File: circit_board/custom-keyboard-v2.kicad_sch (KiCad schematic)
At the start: 1 part

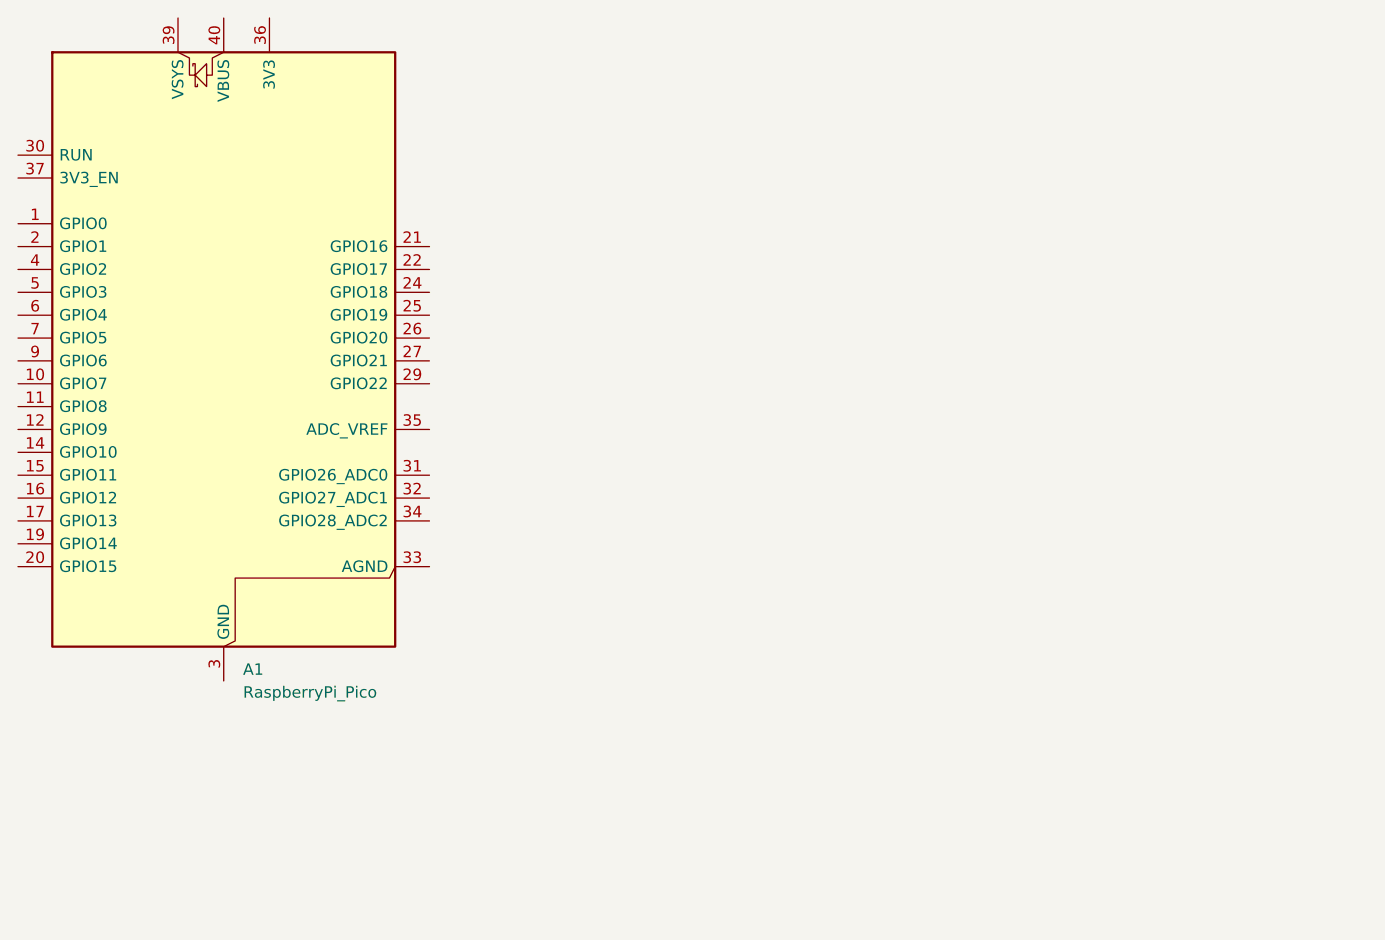
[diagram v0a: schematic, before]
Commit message: Added kicad library for key switches + added a few components into the design
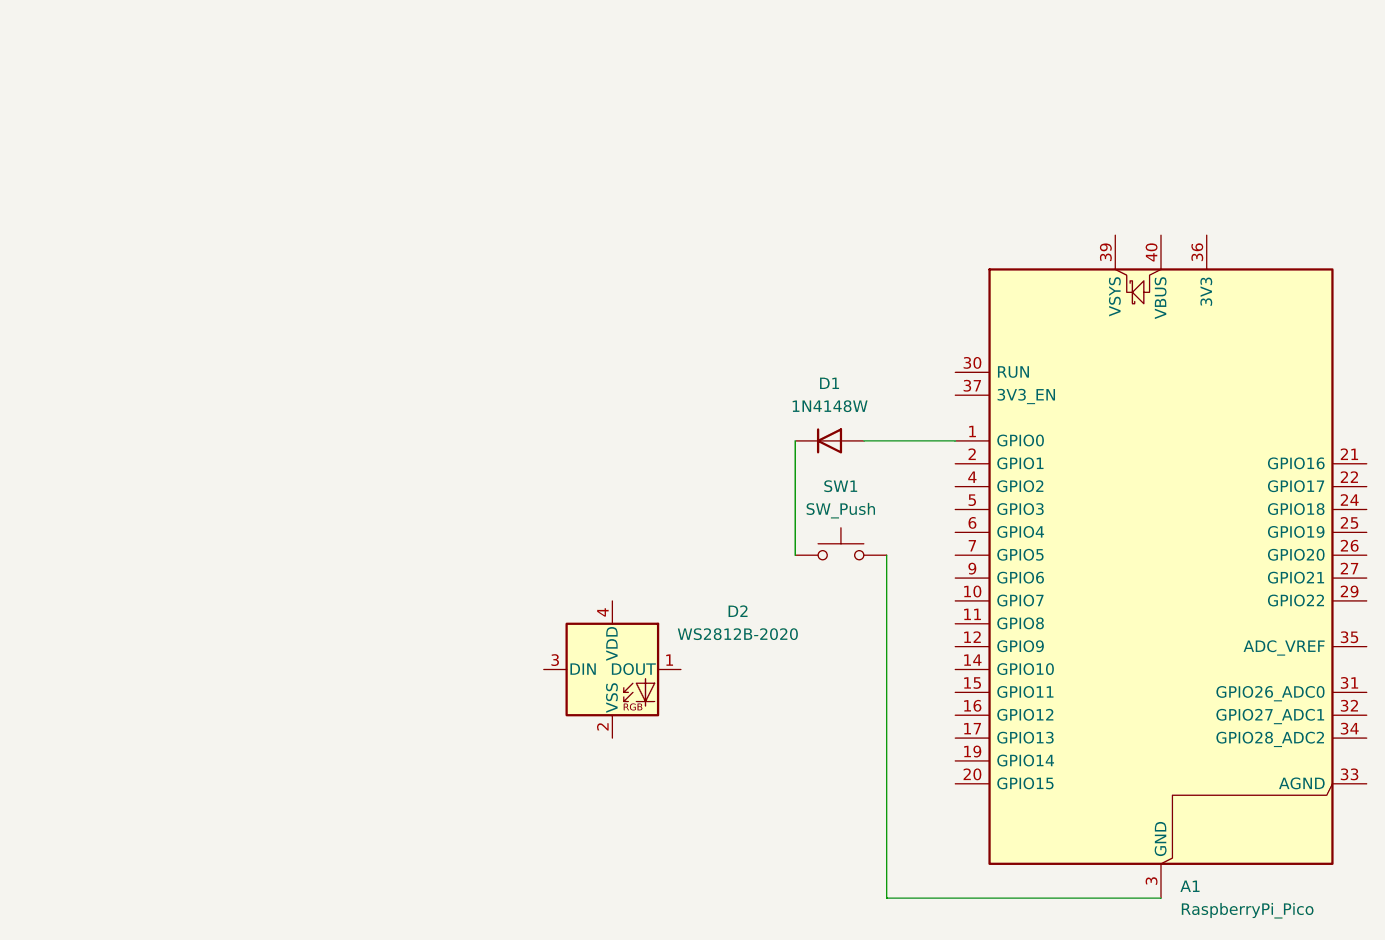
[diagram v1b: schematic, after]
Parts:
- added D1: 1N4148W, Diode_SMD:D_SOD-123, symbol Diode:1N4148W
- added D2: WS2812B-2020, LED_SMD:LED_WS2812B-2020_PLCC4_2.0x2.0mm, symbol LED:WS2812B-2020
- added SW1: SW_Push, MX_V2:Gateron-KS33-Solderable-Template, symbol Switch:SW_Push
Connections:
- net at A1.1 (GPIO0): now also D1.2 (A)
- net at A1.13 (GND), A1.18 (GND), A1.23 (GND)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: now also SW1.2
- new net: D1.1 (K), SW1.1
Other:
- moved on the sheet: A1

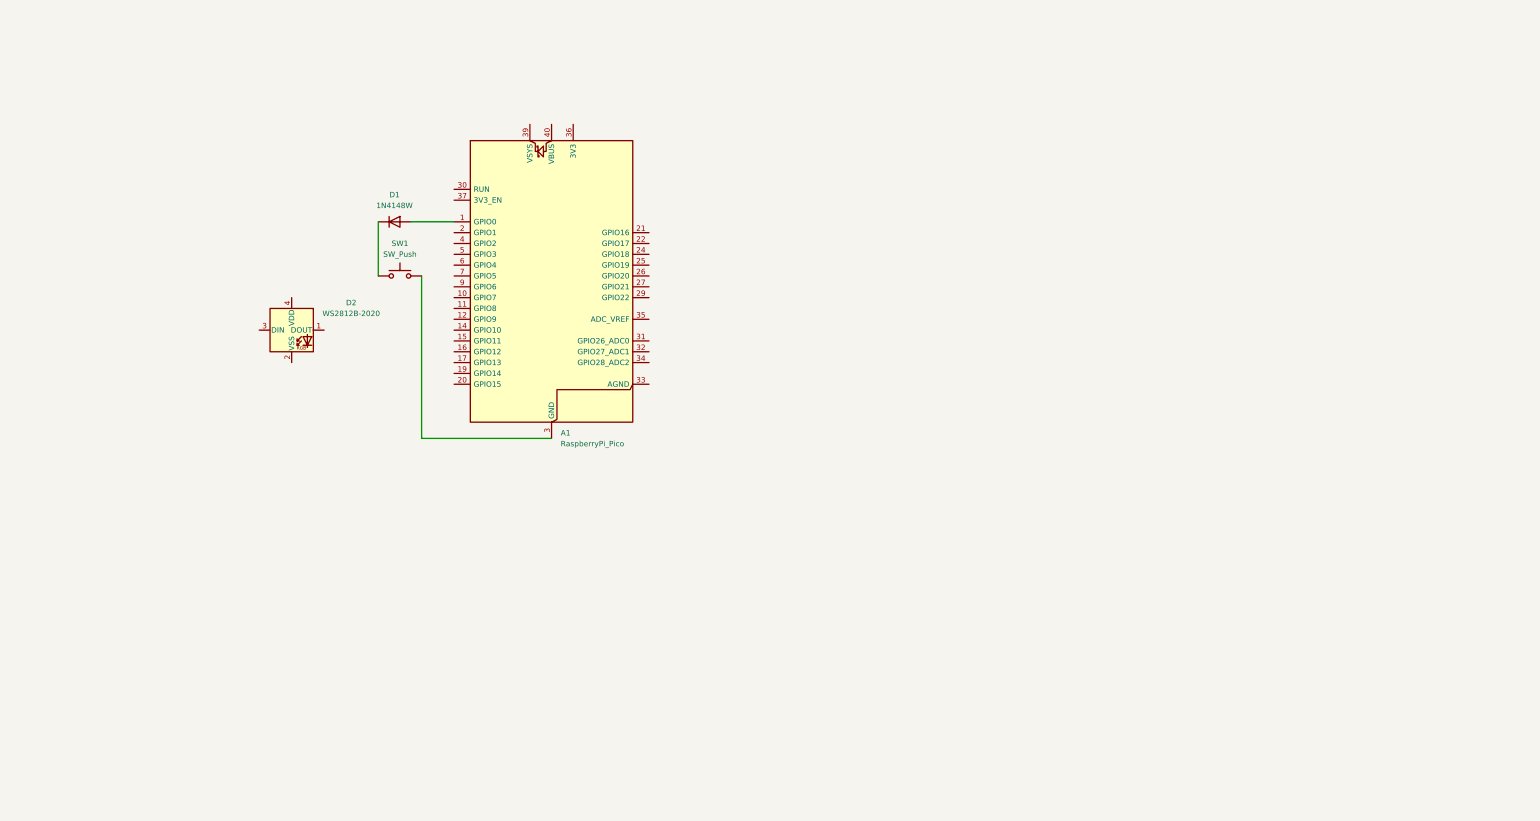
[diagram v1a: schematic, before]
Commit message: Added keyboard matrix to circit schematic
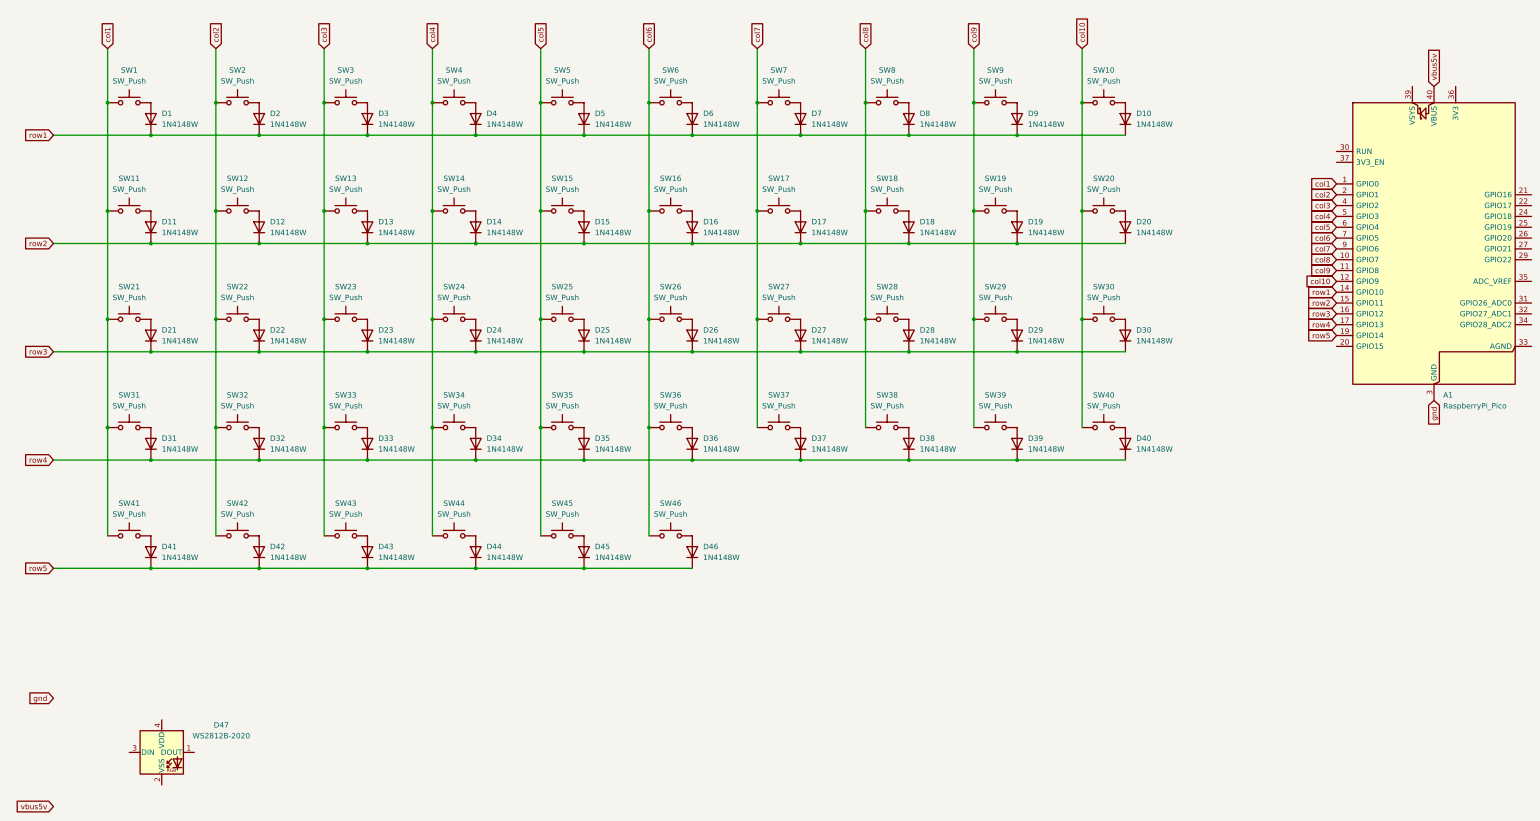
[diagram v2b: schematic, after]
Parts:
- removed D2: WS2812B-2020, LED_SMD:LED_WS2812B-2020_PLCC4_2.0x2.0mm, symbol LED:WS2812B-2020
- added D10, D11, D12, D13, D14, D15, D16, D17, D18, D19, D2, D20, D21, D22, D23, D24, D25, D26, D27, D28, D29, D3, D30, D31, D32, D33, D34, D35, D36, D37, D38, D39, D4, D40, D41, D42, D43, D44, D45, D46, D5, D6, D7, D8, D9: 1N4148W, Diode_SMD:D_SOD-123, symbol Diode:1N4148W
- added D47: WS2812B-2020, LED_SMD:LED_WS2812B-2020_PLCC4_2.0x2.0mm, symbol LED:WS2812B-2020
- added SW10, SW11, SW12, SW13, SW14, SW15, SW16, SW17, SW18, SW19, SW2, SW20, SW21, SW22, SW23, SW24, SW25, SW26, SW27, SW28, SW29, SW3, SW30, SW31, SW32, SW33, SW34, SW35, SW36, SW37, SW38, SW39, SW4, SW40, SW41, SW42, SW43, SW44, SW45, SW46, SW5, SW6, SW7, SW8, SW9: SW_Push, MX_V2:Gateron-KS33-Solderable-Template, symbol Switch:SW_Push
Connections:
- net col1: now reaches SW1.1
- net col1: now also A1.1 (GPIO0), SW11.1, SW21.1, SW31.1, SW41.1; no longer D1.1 (K)
- net at D1.2 (A): now also SW1.2; no longer A1.1 (GPIO0)
- net gnd: now reaches A1.13 (GND), A1.18 (GND), A1.23 (GND), A1.28 (GND), A1.3 (GND), A1.38 (GND), A1.8 (GND)
- net gnd: no longer SW1.2
- net col8: now reaches A1.10 (GPIO7)
- net col8: now also SW18.1, SW28.1, SW38.1, SW8.1
- net col9: now reaches A1.11 (GPIO8)
- net col9: now also SW19.1, SW29.1, SW39.1, SW9.1
- net col10: now reaches A1.12 (GPIO9)
- net col10: now also SW10.1, SW20.1, SW30.1, SW40.1
- net row1: now reaches A1.14 (GPIO10)
- net row1: now also D1.1 (K), D10.1 (K), D2.1 (K), D3.1 (K), D4.1 (K), D5.1 (K), D6.1 (K), D7.1 (K), D8.1 (K), D9.1 (K)
- net row2: now reaches A1.15 (GPIO11)
- net row2: now also D11.1 (K), D12.1 (K), D13.1 (K), D14.1 (K), D15.1 (K), D16.1 (K), D17.1 (K), D18.1 (K), D19.1 (K), D20.1 (K)
- net row3: now reaches A1.16 (GPIO12)
- net row3: now also D21.1 (K), D22.1 (K), D23.1 (K), D24.1 (K), D25.1 (K), D26.1 (K), D27.1 (K), D28.1 (K), D29.1 (K), D30.1 (K)
- net row4: now reaches A1.17 (GPIO13)
- net row4: now also D31.1 (K), D32.1 (K), D33.1 (K), D34.1 (K), D35.1 (K), D36.1 (K), D37.1 (K), D38.1 (K), D39.1 (K), D40.1 (K)
- net row5: now reaches A1.19 (GPIO14)
- net row5: now also D41.1 (K), D42.1 (K), D43.1 (K), D44.1 (K), D45.1 (K), D46.1 (K)
- net col2: now reaches A1.2 (GPIO1)
- net col2: now also SW12.1, SW2.1, SW22.1, SW32.1, SW42.1
- net col3: now reaches A1.4 (GPIO2)
- net col3: now also SW13.1, SW23.1, SW3.1, SW33.1, SW43.1
- net vbus5v: now reaches A1.40 (VBUS)
- net col4: now reaches A1.5 (GPIO3)
- net col4: now also SW14.1, SW24.1, SW34.1, SW4.1, SW44.1
- net col5: now reaches A1.6 (GPIO4)
- net col5: now also SW15.1, SW25.1, SW35.1, SW45.1, SW5.1
- net col6: now reaches A1.7 (GPIO5)
- net col6: now also SW16.1, SW26.1, SW36.1, SW46.1, SW6.1
- net col7: now reaches A1.9 (GPIO6)
- net col7: now also SW17.1, SW27.1, SW37.1, SW7.1
- new net: D14.2 (A), SW14.2
- new net: D32.2 (A), SW32.2
- new net: D34.2 (A), SW34.2
- new net: D43.2 (A), SW43.2
- new net: D42.2 (A), SW42.2
- new net: D23.2 (A), SW23.2
- new net: D20.2 (A), SW20.2
- new net: D41.2 (A), SW41.2
- new net: D16.2 (A), SW16.2
- new net: D38.2 (A), SW38.2
- new net: D45.2 (A), SW45.2
- new net: D21.2 (A), SW21.2
- new net: D15.2 (A), SW15.2
- new net: D35.2 (A), SW35.2
- new net: D10.2 (A), SW10.2
- new net: D18.2 (A), SW18.2
- new net: D26.2 (A), SW26.2
- new net: D33.2 (A), SW33.2
- new net: D24.2 (A), SW24.2
- new net: D46.2 (A), SW46.2
- new net: D37.2 (A), SW37.2
- new net: D6.2 (A), SW6.2
- new net: D29.2 (A), SW29.2
- new net: D12.2 (A), SW12.2
- new net: D9.2 (A), SW9.2
- new net: D31.2 (A), SW31.2
- new net: D8.2 (A), SW8.2
- new net: D2.2 (A), SW2.2
- new net: D27.2 (A), SW27.2
- new net: D40.2 (A), SW40.2
- new net: D25.2 (A), SW25.2
- new net: D13.2 (A), SW13.2
- new net: D28.2 (A), SW28.2
- new net: D19.2 (A), SW19.2
- new net: D36.2 (A), SW36.2
- new net: D30.2 (A), SW30.2
- new net: D22.2 (A), SW22.2
- new net: D4.2 (A), SW4.2
- new net: D44.2 (A), SW44.2
- new net: D17.2 (A), SW17.2
- new net: D5.2 (A), SW5.2
- new net: D11.2 (A), SW11.2
- new net: D7.2 (A), SW7.2
- new net: D39.2 (A), SW39.2
- new net: D3.2 (A), SW3.2
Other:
- moved on the sheet: A1, D1, SW1

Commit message: Added chain of LEDs intended to go under the keys to the schematic
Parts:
- added LED10, LED11, LED12, LED13, LED14, LED15, LED16, LED17, LED18, LED19, LED2, LED20, LED21, LED22, LED23, LED24, LED25, LED26, LED27, LED28, LED29, LED3, LED30, LED31, LED32, LED33, LED34, LED35, LED36, LED37, LED38, LED39, LED4, LED40, LED41, LED42, LED43, LED44, LED45, LED46, LED5, LED6, LED7, LED8, LED9: WS2812B-2020, LED_SMD:LED_WS2812B-2020_PLCC4_2.0x2.0mm, symbol LED:WS2812B-2020
- renumbered D47 to LED1
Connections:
- net gnd: now also LED1.2 (VSS), LED10.2 (VSS), LED11.2 (VSS), LED12.2 (VSS), LED13.2 (VSS), LED14.2 (VSS), LED15.2 (VSS), LED16.2 (VSS), LED17.2 (VSS), LED18.2 (VSS), LED19.2 (VSS), LED2.2 (VSS), LED20.2 (VSS), LED21.2 (VSS), LED22.2 (VSS), LED23.2 (VSS), LED24.2 (VSS), LED25.2 (VSS), LED26.2 (VSS), LED27.2 (VSS), LED28.2 (VSS), LED29.2 (VSS), LED3.2 (VSS), LED30.2 (VSS), LED31.2 (VSS), LED32.2 (VSS), LED33.2 (VSS), LED34.2 (VSS), LED35.2 (VSS), LED36.2 (VSS), LED37.2 (VSS), LED38.2 (VSS), LED39.2 (VSS), LED4.2 (VSS), LED40.2 (VSS), LED41.2 (VSS), LED42.2 (VSS), LED43.2 (VSS), LED44.2 (VSS), LED45.2 (VSS), LED46.2 (VSS), LED5.2 (VSS), LED6.2 (VSS), LED7.2 (VSS), LED8.2 (VSS), LED9.2 (VSS)
- net at LED1.1 (DOUT): now also LED2.3 (DIN)
- net led-data: now reaches LED1.3 (DIN)
- net led-data: now also A1.20 (GPIO15)
- net led-power: now reaches LED1.4 (VDD)
- net led-power: now also LED10.4 (VDD), LED11.4 (VDD), LED12.4 (VDD), LED13.4 (VDD), LED14.4 (VDD), LED15.4 (VDD), LED16.4 (VDD), LED17.4 (VDD), LED18.4 (VDD), LED19.4 (VDD), LED2.4 (VDD), LED20.4 (VDD), LED21.4 (VDD), LED22.4 (VDD), LED23.4 (VDD), LED24.4 (VDD), LED25.4 (VDD), LED26.4 (VDD), LED27.4 (VDD), LED28.4 (VDD), LED29.4 (VDD), LED3.4 (VDD), LED30.4 (VDD), LED31.4 (VDD), LED32.4 (VDD), LED33.4 (VDD), LED34.4 (VDD), LED35.4 (VDD), LED36.4 (VDD), LED37.4 (VDD), LED38.4 (VDD), LED39.4 (VDD), LED4.4 (VDD), LED40.4 (VDD), LED41.4 (VDD), LED42.4 (VDD), LED43.4 (VDD), LED44.4 (VDD), LED45.4 (VDD), LED46.4 (VDD), LED5.4 (VDD), LED6.4 (VDD), LED7.4 (VDD), LED8.4 (VDD), LED9.4 (VDD)
- net vbus5v: no longer names the net of A1.40 (VBUS)
- new net: LED14.1 (DOUT), LED15.3 (DIN)
- new net: LED13.1 (DOUT), LED14.3 (DIN)
- new net: LED19.1 (DOUT), LED20.3 (DIN)
- new net: LED18.1 (DOUT), LED19.3 (DIN)
- new net: LED27.1 (DOUT), LED28.3 (DIN)
- new net: LED26.1 (DOUT), LED27.3 (DIN)
- new net: LED3.1 (DOUT), LED4.3 (DIN)
- new net: LED2.1 (DOUT), LED3.3 (DIN)
- new net: LED32.1 (DOUT), LED33.3 (DIN)
- new net: LED31.1 (DOUT), LED32.3 (DIN)
- new net: LED37.1 (DOUT), LED38.3 (DIN)
- new net: LED36.1 (DOUT), LED37.3 (DIN)
- new net: LED17.1 (DOUT), LED18.3 (DIN)
- new net: LED40.1 (DOUT), LED41.3 (DIN)
- new net: LED39.1 (DOUT), LED40.3 (DIN)
- new net: LED10.1 (DOUT), LED11.3 (DIN)
- new net: LED10.3 (DIN), LED9.1 (DOUT)
- new net: LED30.1 (DOUT), LED31.3 (DIN)
- new net: LED29.1 (DOUT), LED30.3 (DIN)
- new net: LED11.1 (DOUT), LED12.3 (DIN)
- new net: LED35.1 (DOUT), LED36.3 (DIN)
- new net: LED34.1 (DOUT), LED35.3 (DIN)
- new net: LED15.1 (DOUT), LED16.3 (DIN)
- new net: LED45.1 (DOUT), LED46.3 (DIN)
- new net: LED44.1 (DOUT), LED45.3 (DIN)
- new net: LED23.1 (DOUT), LED24.3 (DIN)
- new net: LED22.1 (DOUT), LED23.3 (DIN)
- new net: LED42.1 (DOUT), LED43.3 (DIN)
- new net: LED41.1 (DOUT), LED42.3 (DIN)
- new net: LED43.1 (DOUT), LED44.3 (DIN)
- new net: LED12.1 (DOUT), LED13.3 (DIN)
- new net: LED25.1 (DOUT), LED26.3 (DIN)
- new net: LED24.1 (DOUT), LED25.3 (DIN)
- new net: LED6.1 (DOUT), LED7.3 (DIN)
- new net: LED5.1 (DOUT), LED6.3 (DIN)
- new net: LED33.1 (DOUT), LED34.3 (DIN)
- new net: LED4.1 (DOUT), LED5.3 (DIN)
- new net: LED28.1 (DOUT), LED29.3 (DIN)
- new net: LED8.1 (DOUT), LED9.3 (DIN)
- new net: LED7.1 (DOUT), LED8.3 (DIN)
- new net: LED16.1 (DOUT), LED17.3 (DIN)
- new net: LED21.1 (DOUT), LED22.3 (DIN)
- new net: LED38.1 (DOUT), LED39.3 (DIN)
- new net: LED20.1 (DOUT), LED21.3 (DIN)
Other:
- moved on the sheet: LED1

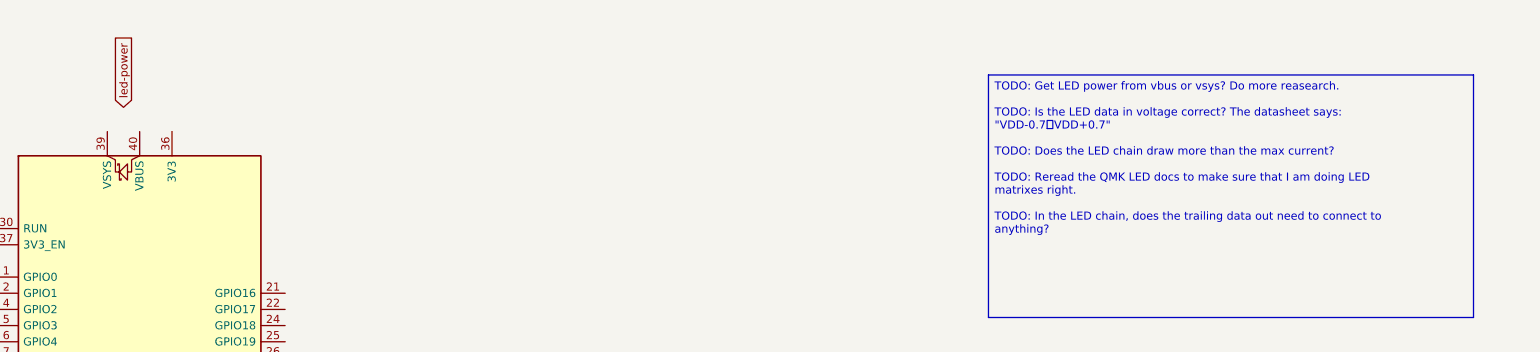
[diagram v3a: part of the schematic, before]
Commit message: LEDs now get power from the Pi Pico's VBUS pin
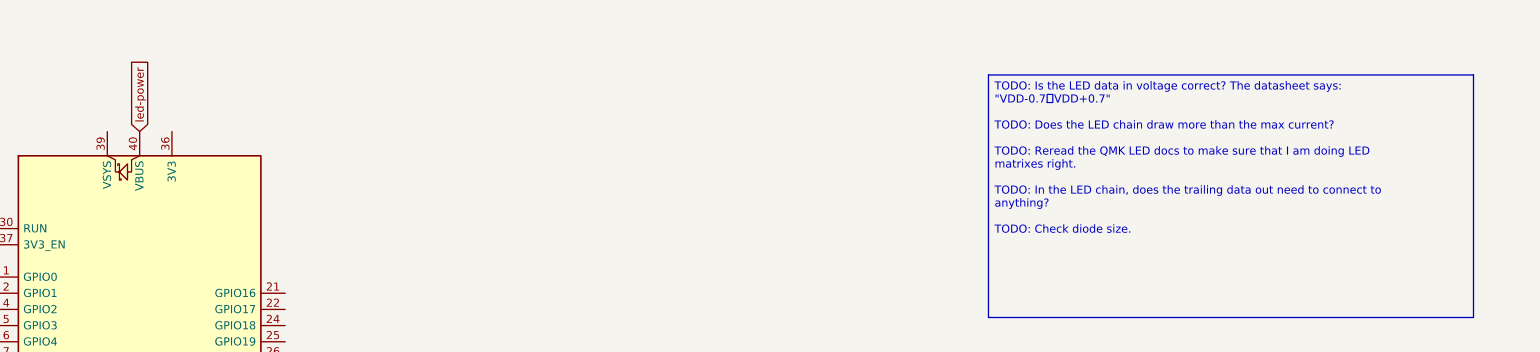
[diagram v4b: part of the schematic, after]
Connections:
- net led-power: now also A1.40 (VBUS)
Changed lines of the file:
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@@
 	(generator_version "9.0")
 	(paper "A2")
-	(text_box "TODO: Get LED power from vbus or vsys? Do more reasearch.\n\nTODO: Is the LED data in voltage correct? The datasheet says: \"VDD-0.7～VDD+0.7\"\n\nTODO: Does the LED chain draw more than the max current?\n\nTODO: Reread the QMK LED docs to make sure that I am doing LED matrixes right.\n\nTODO: In the LED chain, does the trailing data out need to connect to anything?"
+	(text_box "TODO: Is the LED data in voltage correct? The datasheet says: \"VDD-0.7～VDD+0.7\"\n\nTODO: Does the LED chain draw more than the max current?\n\nTODO: Reread the QMK LED docs to make sure that I am doing LED matrixes right.\n\nTODO: In the LED chain, does the trailing data out need to connect to anything?\n\nTODO: Check diode size."
 		(exclude_from_sim no)
 		(at 495.3 25.4 0)
@@
 	(global_label "led-power"
 		(shape input)
-		(at 359.41 30.48 90)
+		(at 361.95 34.29 90)
 		(fields_autoplaced yes)
 		(effects
@@
 		)
 		(property "Intersheetrefs" "${INTERSHEET_REFS}"
-			(at 359.41 17.5163 90)
+			(at 361.95 21.3263 90)
 			(effects
 				(font

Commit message: Possitioned keys on circitboard with spacing of 19mm (may change later)
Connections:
- net col1: no longer SW41.1
- net col2: no longer SW42.1
- net col3: now also SW41.1; no longer SW43.1
- net col4: now also SW42.1; no longer SW44.1
- net col5: now also SW43.1; no longer SW45.1
- net col6: now also SW44.1; no longer SW46.1
- net col7: now also SW45.1
- net col8: now also SW46.1
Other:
- moved on the sheet: D41, D42, D43, D44, D45, D46, SW41, SW42, SW43, SW44, SW45, SW46
